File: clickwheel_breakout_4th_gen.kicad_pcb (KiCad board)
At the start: 2 copper layers, 55.5 x 98.2 mm, 0 parts

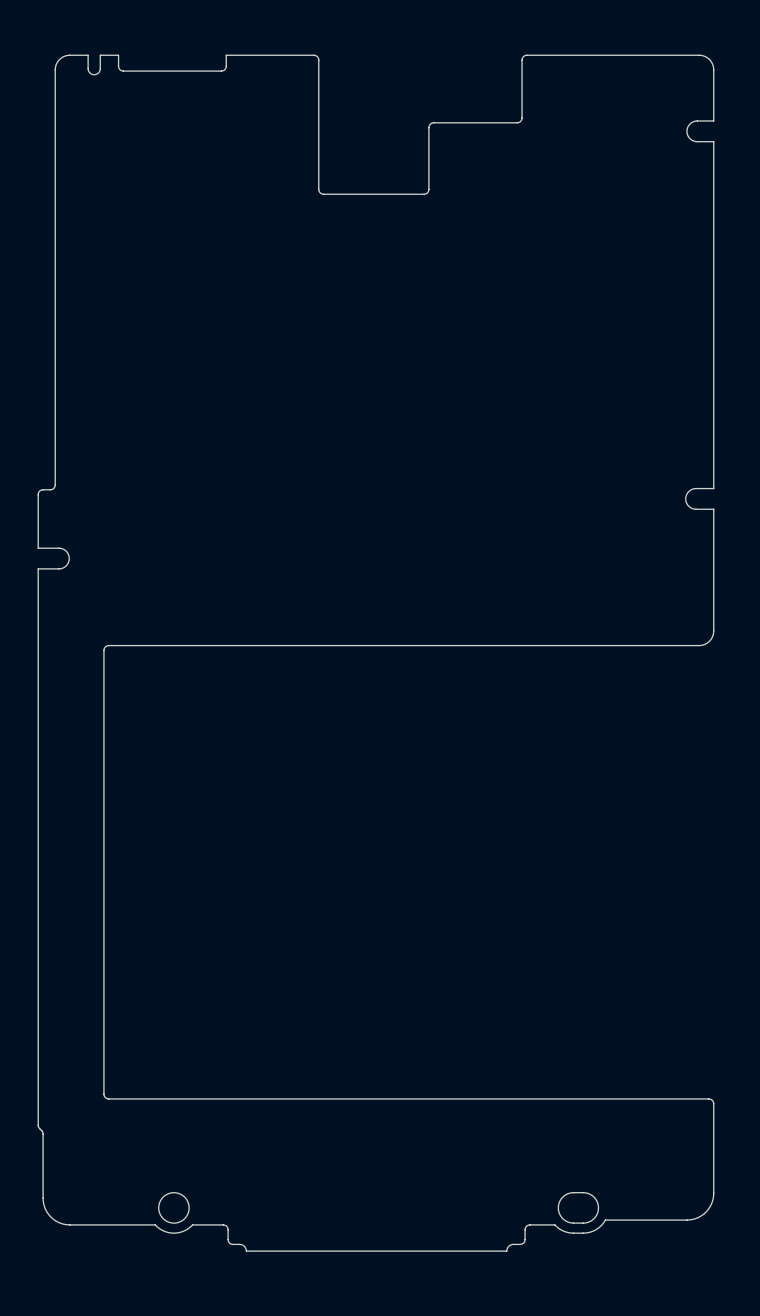
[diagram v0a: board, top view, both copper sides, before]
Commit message: Finish layout of connectors
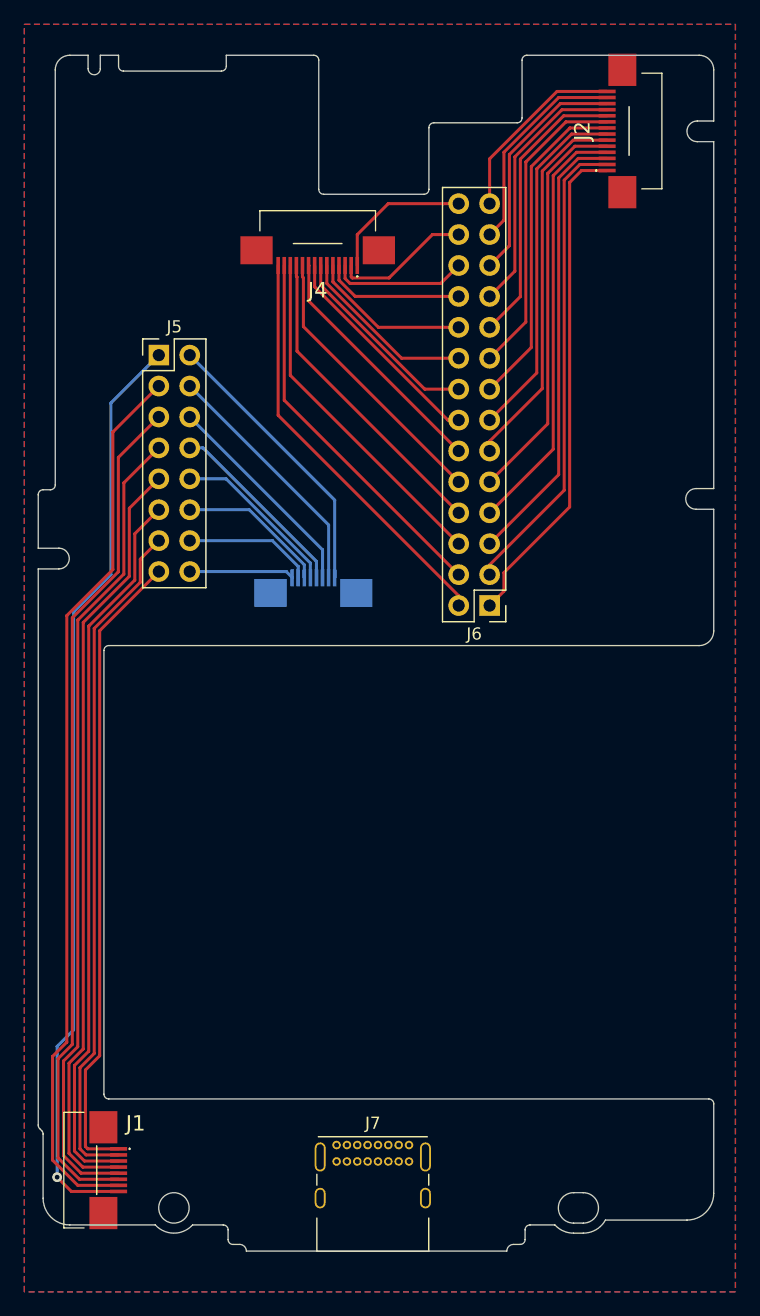
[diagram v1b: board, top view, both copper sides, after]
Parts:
- added J1: SFV8R-2STE1HLF, Gigahawk:SFV8R2STE1HLF, F.Cu at (44.1, 134.8)
- added J2: SFV14R-2STE1HLF, Gigahawk:SFV14R2STE1HLF, F.Cu at (87.8, 49.4)
- added J3: SFV8R-2STE1HLF, Gigahawk:SFV8R2STE1HLF, B.Cu at (61.8, 87.9)
- added J4: SFV14R-2STE1HLF, Gigahawk:SFV14R2STE1HLF, F.Cu at (62.2, 58.7)
- added J5: Conn_02x08_Odd_Even, Connector_PinHeader_2.54mm:PinHeader_2x08_P2.54mm_Vertical, F.Cu at (49.1, 67.8)
- added J6: Conn_02x14_Odd_Even, Connector_PinHeader_2.54mm:PinHeader_2x14_P2.54mm_Vertical, F.Cu at (76.3, 88.4)
- added J7: USB_C_Receptacle_USB2.0, Gigahawk:USB_C_Receptacle_GCT_USB4085, F.Cu at (63.8, 132.7)
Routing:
- net CW_8: track 0.00 -> 76.5 mm, vias 0 -> 1
- net CW_7: track 0.00 -> 73.5 mm
- net CW_6: track 0.00 -> 70.0 mm
- net CW_5: track 0.00 -> 66.5 mm
- net CW_4: track 0.00 -> 63.0 mm
- net CW_3: track 0.00 -> 59.5 mm
- net CW_2: track 0.00 -> 56.0 mm
- net CW_1: track 0.00 -> 52.5 mm
- net HP_1: track 0.00 -> 41.0 mm
- net HP_2: track 0.00 -> 39.0 mm
- net HP_3: track 0.00 -> 37.1 mm
- net HP_4: track 0.00 -> 35.1 mm
- net HP_1MB: track 0.00 -> 34.1 mm
- net HP_5: track 0.00 -> 33.1 mm
- net HP_2MB: track 0.00 -> 31.3 mm
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- added copper zone on B.Cu, net GND
- added copper zone on F.Cu, net GND

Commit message: Add silkscreens
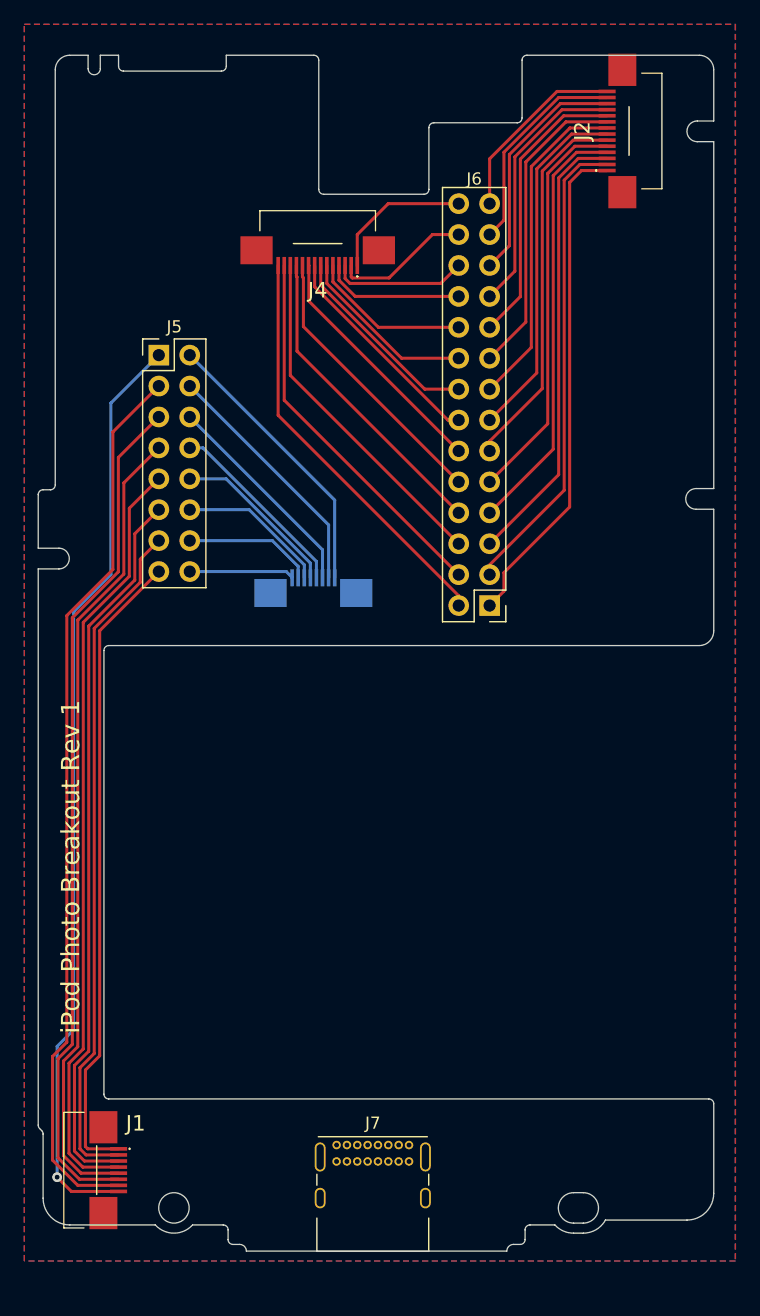
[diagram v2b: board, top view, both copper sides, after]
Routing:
- added copper zone on B.Cu, net (none)
- added copper zone on F.Cu, net (none)
- removed copper zone on B.Cu, net GND
- removed copper zone on F.Cu, net GND
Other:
- board text added: "JLCJLCJLCJLC"
- board text added: "iPod Photo Breakout Rev 1"
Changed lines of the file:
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@@
   (general
     (thickness 0.8)
-    (drawings 85)
+    (drawings 87)
     (tracks 189)
     (zones 0)
@@
       (outputformat 1)
       (mirror false)
-      (drillshape 1)
+      (drillshape 0)
       (scaleselection 1)
-      (outputdirectory ""))
+      (outputdirectory "export/"))
   )
   (net 0 "")
@@
       (effects (font (size 1 1) (thickness 0.15)))
     )
-    (fp_text user %R (at 2.975 4.025) (layer F.Fab)
-      (effects (font (size 1 1) (thickness 0.15)))
-    )
-    (fp_text user "PCB Edge" (at 2.975 6.1) (layer Dwgs.User)
-      (effects (font (size 0.5 0.5) (thickness 0.1)))
-    )
     (fp_line (start -0.025 6.1) (end 5.975 6.1) (layer F.Fab) (width 0.1))
     (fp_line (start 8.25 -1.06) (end 8.25 9.11) (layer F.CrtYd) (width 0.05))
@@
     (fp_line (start -1.5 8.61) (end 7.45 8.61) (layer F.Fab) (width 0.1))
     (fp_line (start -1.5 -0.56) (end 7.45 -0.56) (layer F.Fab) (width 0.1))
+    (fp_text user %R (at 2.975 4.025) (layer F.Fab)
+      (effects (font (size 1 1) (thickness 0.15)))
+    )
+    (fp_text user "PCB Edge" (at 2.975 6.1) (layer Dwgs.User)
+      (effects (font (size 0.5 0.5) (thickness 0.1)))
+    )
     (pad S1 thru_hole oval (at 7.3 4.36) (size 0.9 1.7) (drill oval 0.6 1.4) (layers *.Cu *.Mask)
       (net 53 "Net-(J7-PadS1)"))
@@
     (descr "Through hole straight pin header, 2x14, 2.54mm pitch, double rows")
     (tags "Through hole pin header THT 2x14 2.54mm double row")
-    (fp_text reference J6 (at 1.27 -2.33) (layer F.SilkS)
+    (fp_text reference J6 (at 1.27 35.052) (layer F.SilkS)
       (effects (font (size 1 1) (thickness 0.15)))
     )
     (fp_text value Conn_02x14_Odd_Even (at 1.27 35.35) (layer F.Fab)
-      (effects (font (size 1 1) (thickness 0.15)))
-    )
-    (fp_text user %R (at 1.27 16.51 90) (layer F.Fab)
       (effects (font (size 1 1) (thickness 0.15)))
     )
@@
     (fp_line (start 4.35 34.8) (end 4.35 -1.8) (layer F.CrtYd) (width 0.05))
     (fp_line (start 4.35 -1.8) (end -1.8 -1.8) (layer F.CrtYd) (width 0.05))
+    (fp_text user %R (at 1.27 16.51 90) (layer F.Fab)
+      (effects (font (size 1 1) (thickness 0.15)))
+    )
     (pad 28 thru_hole oval (at 2.54 33.02 180) (size 1.7 1.7) (drill 1) (layers *.Cu *.Mask)
       (net 37 HP_14MB))
@@
       (effects (font (size 1 1) (thickness 0.15)))
     )
-    (fp_text user %R (at 1.27 8.89 90) (layer F.Fab)
-      (effects (font (size 1 1) (thickness 0.15)))
-    )
     (fp_line (start 0 -1.27) (end 3.81 -1.27) (layer F.Fab) (width 0.1))
     (fp_line (start 3.81 -1.27) (end 3.81 19.05) (layer F.Fab) (width 0.1))
@@
     (fp_line (start 4.35 19.55) (end 4.35 -1.8) (layer F.CrtYd) (width 0.05))
     (fp_line (start 4.35 -1.8) (end -1.8 -1.8) (layer F.CrtYd) (width 0.05))
+    (fp_text user %R (at 1.27 8.89 90) (layer F.Fab)
+      (effects (font (size 1 1) (thickness 0.15)))
+    )
     (pad 16 thru_hole oval (at 2.54 17.78) (size 1.7 1.7) (drill 1) (layers *.Cu *.Mask)
       (net 36 CW_1MB))
@@
       (effects (font (size 1.27 1.27) (thickness 0.254)))
     )
-    (fp_arc (start -3.25 -2.675) (end -3.2 -2.675) (angle 180) (layer F.SilkS) (width 0.1))
-    (fp_arc (start -3.25 -2.675) (end -3.3 -2.675) (angle 180) (layer F.SilkS) (width 0.1))
-    (fp_text user %R (at 0 0) (layer F.Fab)
-      (effects (font (size 1.27 1.27) (thickness 0.254)))
-    )
     (fp_line (start -4.75 -1.475) (end 4.75 -1.475) (layer F.Fab) (width 0.2))
     (fp_line (start 4.75 -1.475) (end 4.75 2.725) (layer F.Fab) (width 0.2))
@@
     (fp_line (start -3.2 -2.675) (end -3.2 -2.675) (layer F.SilkS) (width 0.1))
     (fp_line (start -2 0.025) (end 2 0.025) (layer F.SilkS) (width 0.12))
+    (fp_arc (start -3.25 -2.675) (end -3.2 -2.675) (angle 180) (layer F.SilkS) (width 0.1))
+    (fp_arc (start -3.25 -2.675) (end -3.3 -2.675) (angle 180) (layer F.SilkS) (width 0.1))
+    (fp_text user %R (at 0 0) (layer F.Fab)
+      (effects (font (size 1.27 1.27) (thickness 0.254)))
+    )
     (pad 14 smd rect (at 3.25 -1.775 180) (size 0.3 1.4) (layers F.Cu F.Paste F.Mask)
       (net 51 HP_1MB))
@@
       (effects (font (size 1.27 1.27) (thickness 0.254)) (justify mirror))
     )
-    (fp_arc (start -1.75 2.675) (end -1.7 2.675) (angle -180) (layer B.SilkS) (width 0.1))
-    (fp_arc (start -1.75 2.675) (end -1.8 2.675) (angle -180) (layer B.SilkS) (width 0.1))
-    (fp_text user %R (at 0 0) (layer B.Fab)
-      (effects (font (size 1.27 1.27) (thickness 0.254)) (justify mirror))
-    )
     (fp_line (start -2 -0.025) (end 2 -0.025) (layer B.SilkS) (width 0.12))
     (fp_line (start -1.7 2.675) (end -1.7 2.675) (layer B.SilkS) (width 0.1))
@@
     (fp_line (start 4.75 1.475) (end 4.75 -2.725) (layer B.Fab) (width 0.2))
     (fp_line (start -4.75 1.475) (end 4.75 1.475) (layer B.Fab) (width 0.2))
+    (fp_arc (start -1.75 2.675) (end -1.7 2.675) (angle -180) (layer B.SilkS) (width 0.1))
+    (fp_arc (start -1.75 2.675) (end -1.8 2.675) (angle -180) (layer B.SilkS) (width 0.1))
+    (fp_text user %R (at 0 0) (layer B.Fab)
+      (effects (font (size 1.27 1.27) (thickness 0.254)) (justify mirror))
+    )
     (pad M2 smd rect (at 3.525 0.525 90) (size 2.3 2.65) (layers B.Cu B.Paste B.Mask)
       (net 27 "Net-(J3-PadM2)"))
@@
       (effects (font (size 1.27 1.27) (thickness 0.254)))
     )
-    (fp_arc (start -1.75 -2.675) (end -1.7 -2.675) (angle 180) (layer F.SilkS) (width 0.1))
-    (fp_arc (start -1.75 -2.675) (end -1.8 -2.675) (angle 180) (layer F.SilkS) (width 0.1))
-    (fp_text user %R (at 0 0 90) (layer F.Fab)
-      (effects (font (size 1.27 1.27) (thickness 0.254)))
-    )
     (fp_line (start -2 0.025) (end 2 0.025) (layer F.SilkS) (width 0.12))
     (fp_line (start -1.7 -2.675) (end -1.7 -2.675) (layer F.SilkS) (width 0.1))
@@
     (fp_line (start 4.75 -1.475) (end 4.75 2.725) (layer F.Fab) (width 0.2))
     (fp_line (start -4.75 -1.475) (end 4.75 -1.475) (layer F.Fab) (width 0.2))
+    (fp_arc (start -1.75 -2.675) (end -1.7 -2.675) (angle 180) (layer F.SilkS) (width 0.1))
+    (fp_arc (start -1.75 -2.675) (end -1.8 -2.675) (angle 180) (layer F.SilkS) (width 0.1))
+    (fp_text user %R (at 0 0 90) (layer F.Fab)
+      (effects (font (size 1.27 1.27) (thickness 0.254)))
+    )
     (pad M2 smd rect (at 3.525 -0.525) (size 2.3 2.65) (layers F.Cu F.Paste F.Mask)
       (net 3 "Net-(J1-PadM2)"))
@@
       (effects (font (size 1.27 1.27) (thickness 0.254)))
     )
-    (fp_arc (start -3.25 -2.675) (end -3.2 -2.675) (angle 180) (layer F.SilkS) (width 0.1))
-    (fp_arc (start -3.25 -2.675) (end -3.3 -2.675) (angle 180) (layer F.SilkS) (width 0.1))
-    (fp_text user %R (at 0 0 90) (layer F.Fab)
-      (effects (font (size 1.27 1.27) (thickness 0.254)))
-    )
     (fp_line (start -4.75 -1.475) (end 4.75 -1.475) (layer F.Fab) (width 0.2))
     (fp_line (start 4.75 -1.475) (end 4.75 2.725) (layer F.Fab) (width 0.2))
@@
     (fp_line (start -3.2 -2.675) (end -3.2 -2.675) (layer F.SilkS) (width 0.1))
     (fp_line (start -2 0.025) (end 2 0.025) (layer F.SilkS) (width 0.12))
+    (fp_arc (start -3.25 -2.675) (end -3.2 -2.675) (angle 180) (layer F.SilkS) (width 0.1))
+    (fp_arc (start -3.25 -2.675) (end -3.3 -2.675) (angle 180) (layer F.SilkS) (width 0.1))
+    (fp_text user %R (at 0 0 90) (layer F.Fab)
+      (effects (font (size 1.27 1.27) (thickness 0.254)))
+    )
     (pad 14 smd rect (at 3.25 -1.775 90) (size 0.3 1.4) (layers F.Cu F.Paste F.Mask)
       (net 13 HP_14))
@@
       (rotate (xyz -90 0 0))
     )
+  )
+  (gr_text "JLCJLCJLCJLC\n" (at 41.91 109.855 90) (layer B.SilkS)
+    (effects (font (size 0.8 0.8) (thickness 0.15)))
+  )
+  (gr_text "iPod Photo Breakout Rev 1\n" (at 41.91 109.855 90) (layer F.SilkS)
+    (effects (font (size 1.5 1.5) (thickness 0.3)))
   )
   (gr_arc (start 78.59 48.33) (end 78.59 48.73) (angle -90) (layer Edge.Cuts) (width 0.05))
@@
   (segment (start 59.452 71.517) (end 73.787 85.852) (width 0.25) (layer F.Cu) (net 52))
   (segment (start 59.452 60.452) (end 59.452 71.517) (width 0.25) (layer F.Cu) (net 52))
-  (zone (net 55) (net_name GND) (layer F.Cu) (hatch edge 0.508)
+  (zone (net 0) (net_name "") (layer B.Cu) (hatch edge 0.508)
     (connect_pads (clearance 0.508))
     (min_thickness 0.254)
-    (fill (arc_segments 32) (thermal_gap 0.508) (thermal_bridge_width 0.508))
+    (fill yes (arc_segments 32) (thermal_gap 0.508) (thermal_bridge_width 0.508))
     (polygon
       (pts
-        (xy 96.52 144.78) (xy 38.1 144.78) (xy 38.1 40.64) (xy 96.52 40.64)
+        (xy 96.52 142.24) (xy 38.1 142.24) (xy 38.1 40.64) (xy 96.52 40.64)
       )
     )
   )
-  (zone (net 55) (net_name GND) (layer B.Cu) (hatch edge 0.508)
+  (zone (net 0) (net_name "") (layer F.Cu) (hatch edge 0.508)
     (connect_pads (clearance 0.508))
     (min_thickness 0.254)
-    (fill (arc_segments 32) (thermal_gap 0.508) (thermal_bridge_width 0.508))
+    (fill yes (arc_segments 32) (thermal_gap 0.508) (thermal_bridge_width 0.508))
     (polygon
       (pts
-        (xy 96.52 144.78) (xy 38.1 144.78) (xy 38.1 40.64) (xy 96.52 40.64)
+        (xy 96.52 142.24) (xy 38.1 142.24) (xy 38.1 40.64) (xy 96.52 40.64)
       )
     )

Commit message: Add known clickwheel signal names
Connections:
- net CW_1 renamed CW_VBAT
- net CW_1MB renamed CW_VBATMB
- net CW_2 renamed CW_SCL
- net CW_2MB renamed CW_SCLMB
- net CW_3 renamed CW_EN2
- net CW_3MB renamed CW_EN2MB
- net CW_6 renamed CW_SDA
- net CW_6MB renamed CW_SDAMB
- net CW_7 renamed CW_EN1
- net CW_7MB renamed CW_EN1MB
- net CW_8 renamed CW_GND
- net CW_8MB renamed CW_GNDMB
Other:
- board text added: "EN1"
- board text added: "EN2"
- board text added: "GND"
- board text added: "NOTE: CLICKWHEEL IS NOT AN I2C DEVICE. See https://jasongarr.wordpress.com/project-pages/ipod-clickwheel-hack/ for more info"
- board text added: "SCL"
- board text added: "SDA"
- board text added: "VBAT"
